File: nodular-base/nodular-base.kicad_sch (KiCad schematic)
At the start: 30 parts, among them J11 Conn_01x08_Pin, SW1 SW_Push, SW2 SW_Push, SW3 SW_Push, U1 ESP32-S3-PICO-1-N8R2

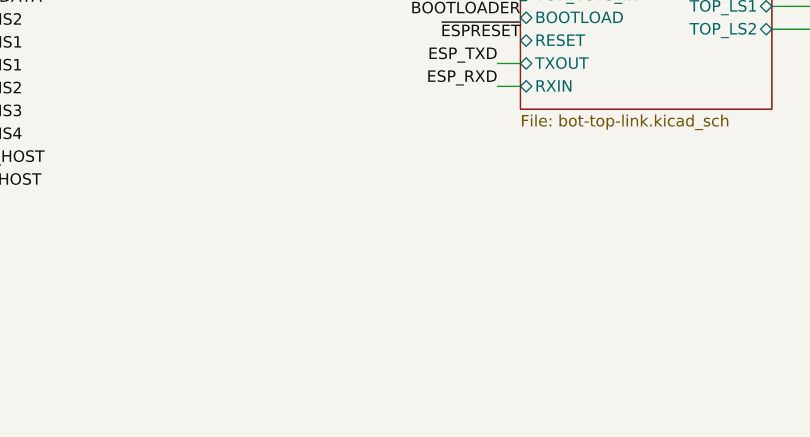
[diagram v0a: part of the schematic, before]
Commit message: Add baseline art (bart), add stencil alignment holes, complete BOM, prepare for proto order
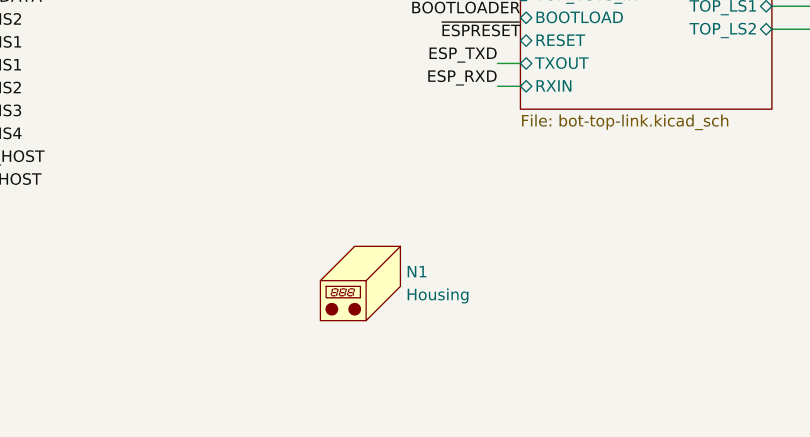
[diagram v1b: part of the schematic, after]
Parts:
- added N1: Housing, nodular:bartholomew, symbol Mechanical:Housing
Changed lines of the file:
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@@
+    )
+  )
+  (symbol (lib_id "Mechanical:Housing") (at 139.7 182.88 0) (unit 1)
+    (in_bom yes) (on_board yes) (dnp no) (fields_autoplaced)
+    (property "Reference" "N1" (at 143.51 181.9275 0)
+      (effects (font (size 1.27 1.27)) (justify left))
+    )
+    (property "Value" "Housing" (at 143.51 184.4675 0)
+      (effects (font (size 1.27 1.27)) (justify left))
+    )
+    (property "Footprint" "nodular:bartholomew" (at 140.97 181.61 0)
+      (effects (font (size 1.27 1.27)) hide)
+    )
+    (property "Datasheet" "~" (at 140.97 181.61 0)
+      (effects (font (size 1.27 1.27)) hide)
+    )
+    (instances
+      (project "nodular-base"
+        (path "/6dcb0502-87e2-4c28-9ce8-81aab8925f06"
+          (reference "N1") (unit 1)
+        )
+      )
     )
   )

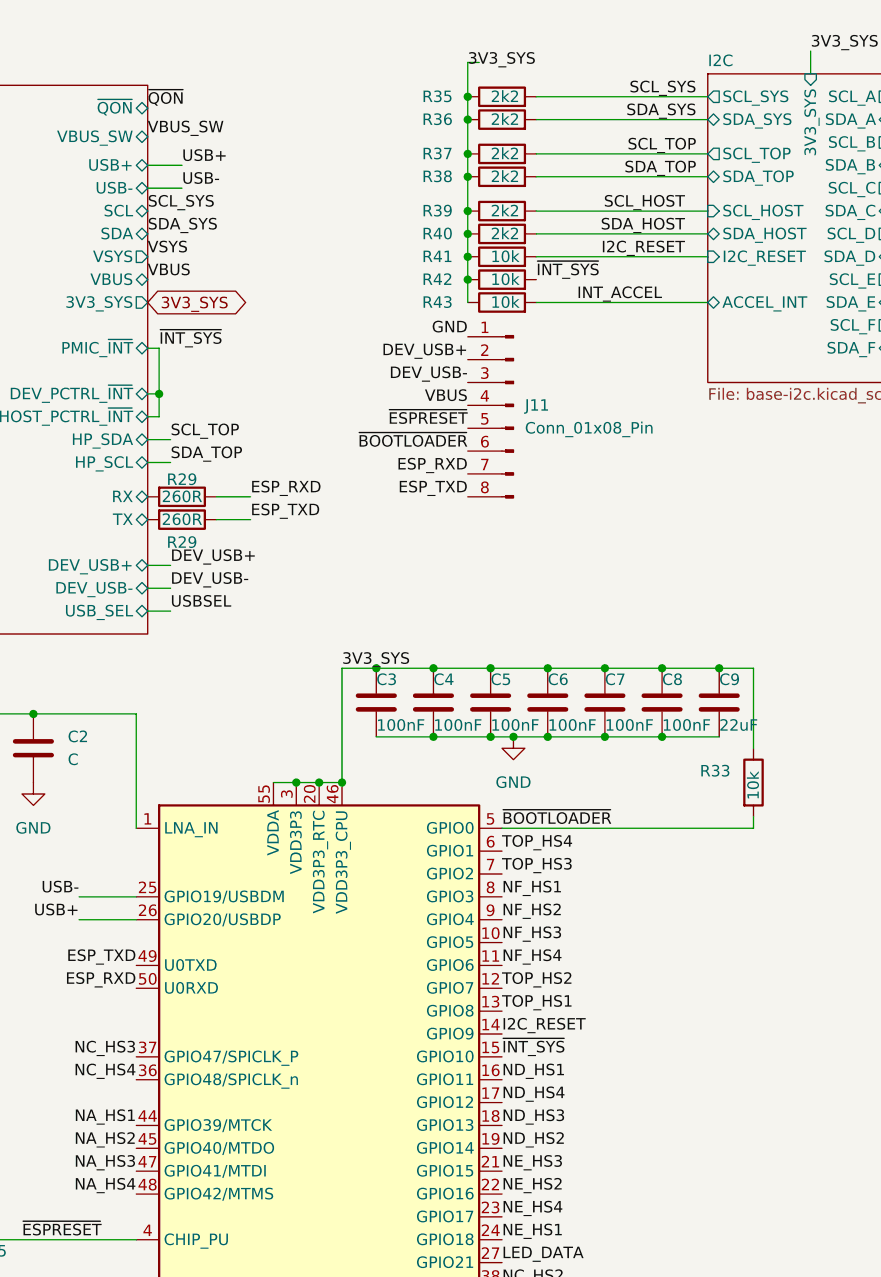
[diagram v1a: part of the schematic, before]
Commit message: Modify base board: - Fix ESP32 strapping pins state - Remove 3/6 M3 standoffs - Change to LGA-style pads on ESP32 - Modify SFP mechanical pads to not be plated - Add larger mechanical pads with more solder paste surface to USB-C connectors
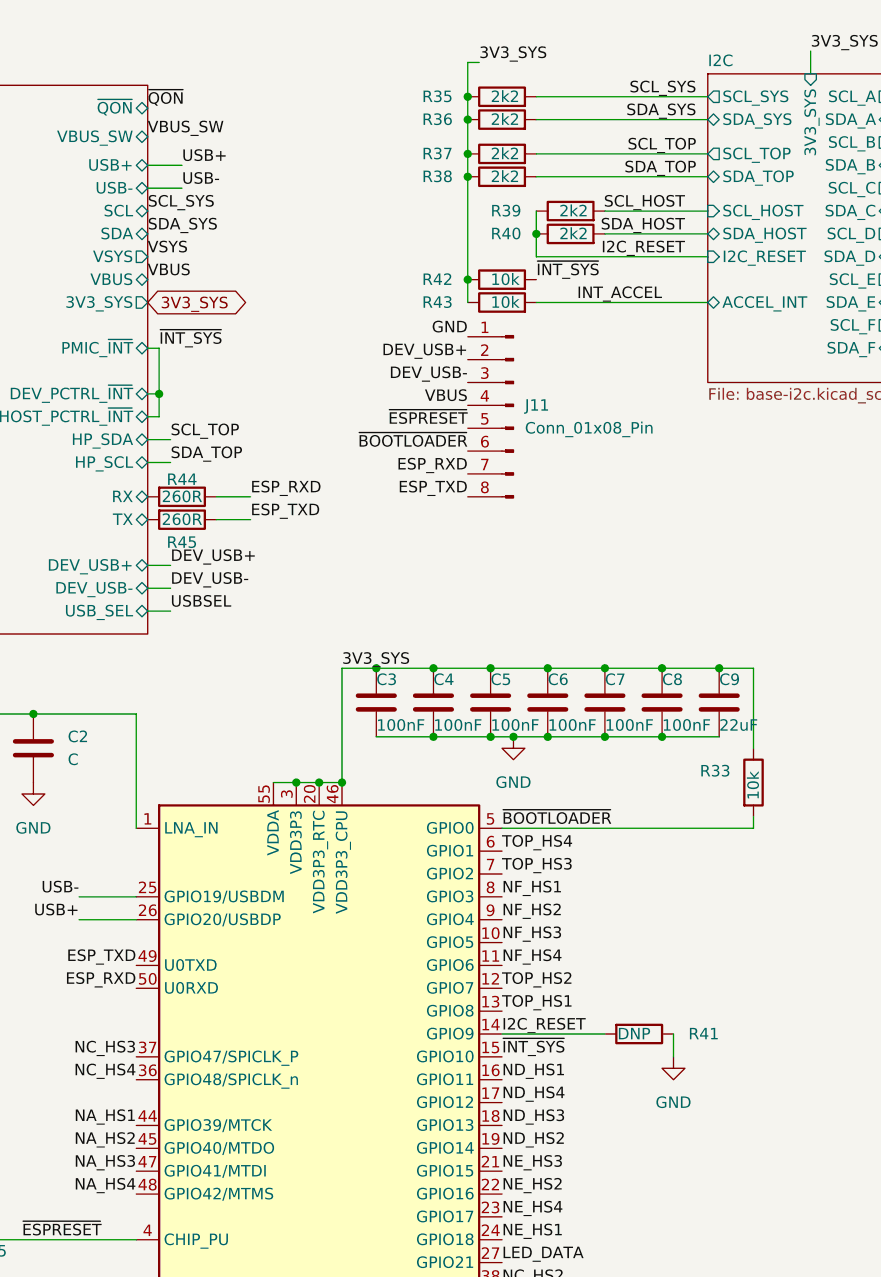
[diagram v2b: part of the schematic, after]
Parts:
- R41: value 10k -> DNP
- U1: footprint Package_DFN_QFN:QFN-56-1EP_7x7mm_P0.4mm_EP4x4mm -> nodular:LGA56-1EP_7x7mm_P0.4mm_EP4x4mm
- renumbered R29 to R44, R29 to R45
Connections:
- net 3V3_SYS: no longer R39.1, R40.1, R41.1
- net GND: now also R41.1
- net I2C_RESET: now also R39.1, R40.1
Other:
- moved on the sheet: R39, R40, R41
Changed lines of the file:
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@@
   (junction (at 76.2 99.06) (diameter 0) (color 0 0 0 0)
   )
-  (junction (at 90.17 38.1) (diameter 0) (color 0 0 0 0)
-  )
   (junction (at 105.41 93.98) (diameter 0) (color 0 0 0 0)
   )
@@
   (junction (at 90.17 22.86) (diameter 0) (color 0 0 0 0)
   )
-  (junction (at 90.17 35.56) (diameter 0) (color 0 0 0 0)
-  )
   (junction (at 111.76 93.98) (diameter 0) (color 0 0 0 0)
   )
   (junction (at 73.66 99.06) (diameter 0) (color 0 0 0 0)
   )
-  (junction (at 90.17 40.64) (diameter 0) (color 0 0 0 0)
-  )
   (junction (at 99.06 93.98) (diameter 0) (color 0 0 0 0)
   )
@@
   )
   (junction (at 86.36 86.36) (diameter 0) (color 0 0 0 0)
+  )
+  (junction (at 97.79 38.1) (diameter 0) (color 0 0 0 0)
   )
   (junction (at 118.11 86.36) (diameter 0) (color 0 0 0 0)
@@
     (stroke (width 0) (type default))
   )
+  (wire (pts (xy 97.79 38.1) (xy 97.79 40.64))
+    (stroke (width 0) (type default))
+  )
   (wire (pts (xy 92.71 93.98) (xy 95.25 93.98))
     (stroke (width 0) (type default))
@@
     (stroke (width 0) (type default))
   )
+  (wire (pts (xy 97.79 35.56) (xy 97.79 38.1))
+    (stroke (width 0) (type default))
+  )
   (wire (pts (xy 153.67 158.75) (xy 156.21 158.75))
     (stroke (width 0) (type default))
@@
     (stroke (width 0) (type default))
   )
-  (wire (pts (xy 97.79 35.56) (xy 116.84 35.56))
+  (wire (pts (xy 105.41 35.56) (xy 116.84 35.56))
     (stroke (width 0) (type default))
   )
@@
     (stroke (width 0) (type default))
   )
-  (wire (pts (xy 90.17 31.75) (xy 90.17 35.56))
-    (stroke (width 0) (type default))
-  )
   (wire (pts (xy 185.42 92.71) (xy 205.74 92.71))
     (stroke (width 0) (type default))
@@
     (stroke (width 0) (type default))
   )
+  (wire (pts (xy 113.03 127) (xy 113.03 129.54))
+    (stroke (width 0) (type default))
+  )
   (wire (pts (xy 184.15 149.86) (xy 205.74 149.86))
     (stroke (width 0) (type default))
@@
     (stroke (width 0) (type default))
   )
-  (wire (pts (xy 90.17 40.64) (xy 90.17 43.18))
+  (wire (pts (xy 90.17 31.75) (xy 90.17 43.18))
     (stroke (width 0) (type default))
   )
@@
     (stroke (width 0) (type default))
   )
-  (wire (pts (xy 97.79 38.1) (xy 116.84 38.1))
+  (wire (pts (xy 105.41 38.1) (xy 116.84 38.1))
     (stroke (width 0) (type default))
   )
@@
     (stroke (width 0) (type default))
   )
-  (wire (pts (xy 90.17 35.56) (xy 90.17 38.1))
-    (stroke (width 0) (type default))
-  )
   (wire (pts (xy 185.42 26.67) (xy 205.74 26.67))
     (stroke (width 0) (type default))
@@
     (stroke (width 0) (type default))
   )
-  (wire (pts (xy 90.17 38.1) (xy 90.17 40.64))
-    (stroke (width 0) (type default))
-  )
   (wire (pts (xy 137.16 50.8) (xy 157.48 50.8))
     (stroke (width 0) (type default))
@@
     (stroke (width 0) (type default))
   )
+  (wire (pts (xy 93.98 127) (xy 105.41 127))
+    (stroke (width 0) (type default))
+  )
   (wire (pts (xy 185.42 39.37) (xy 205.74 39.37))
     (stroke (width 0) (type default))
@@
     (effects (font (size 1.27 1.27)) (justify right bottom))
   )
-  (label "3V3_SYS" (at 90.17 19.685 0) (fields_autoplaced)
+  (label "3V3_SYS" (at 91.44 19.05 0) (fields_autoplaced)
     (effects (font (size 1.27 1.27)) (justify left bottom))
   )
@@
     )
   )
-  (symbol (lib_id "Device:R") (at 93.98 40.64 90) (unit 1)
-    (in_bom yes) (on_board yes) (dnp no)
-    (property "Reference" "R41" (at 85.09 40.64 90)
-      (effects (font (size 1.27 1.27)) (justify right))
-    )
-    (property "Value" "10k" (at 92.71 40.64 90)
-      (effects (font (size 1.27 1.27)) (justify right))
-    )
-    (property "Footprint" "Resistor_SMD:R_0402_1005Metric" (at 93.98 42.418 90)
-      (effects (font (size 1.27 1.27)) hide)
-    )
-    (property "Datasheet" "~" (at 93.98 40.64 0)
+  (symbol (lib_id "Device:R") (at 109.22 127 270) (unit 1)
+    (in_bom yes) (on_board yes) (dnp no)
+    (property "Reference" "R41" (at 118.11 127 90)
+      (effects (font (size 1.27 1.27)) (justify right))
+    )
+    (property "Value" "DNP" (at 110.49 127 90)
+      (effects (font (size 1.27 1.27)) (justify right))
+    )
+    (property "Footprint" "Resistor_SMD:R_0402_1005Metric" (at 109.22 125.222 90)
+      (effects (font (size 1.27 1.27)) hide)
+    )
+    (property "Datasheet" "~" (at 109.22 127 0)
       (effects (font (size 1.27 1.27)) hide)
     )
@@
   (symbol (lib_id "Device:R") (at 58.42 67.31 270) (unit 1)
     (in_bom yes) (on_board yes) (dnp no)
-    (property "Reference" "R29" (at 58.42 65.405 90)
+    (property "Reference" "R44" (at 58.42 65.405 90)
       (effects (font (size 1.27 1.27)))
     )
@@
     (instances
       (project "nodular-base"
-        (path "/6dcb0502-87e2-4c28-9ce8-81aab8925f06/febeaf27-8aaa-445d-863a-3f8ee5c51d55"
-          (reference "R29") (unit 1)
-        )
         (path "/6dcb0502-87e2-4c28-9ce8-81aab8925f06"
           (reference "R44") (unit 1)
@@
     )
   )
+  (symbol (lib_id "power:GND") (at 113.03 129.54 0) (unit 1)
+    (in_bom yes) (on_board yes) (dnp no) (fields_autoplaced)
+    (property "Reference" "#PWR072" (at 113.03 135.89 0)
+      (effects (font (size 1.27 1.27)) hide)
+    )
+    (property "Value" "GND" (at 113.03 134.62 0)
+      (effects (font (size 1.27 1.27)))
+    )
+    (property "Footprint" "" (at 113.03 129.54 0)
+      (effects (font (size 1.27 1.27)) hide)
+    )
+    (property "Datasheet" "" (at 113.03 129.54 0)
+      (effects (font (size 1.27 1.27)) hide)
+    )
+    (pin "1")
+    (instances
+      (project "nodular-base"
+        (path "/6dcb0502-87e2-4c28-9ce8-81aab8925f06"
+          (reference "#PWR072") (unit 1)
+        )
+      )
+    )
+  )
   (symbol (lib_id "Device:R") (at 93.98 43.18 90) (unit 1)
     (in_bom yes) (on_board yes) (dnp no)
@@
     )
   )
-  (symbol (lib_id "Device:R") (at 93.98 38.1 90) (unit 1)
-    (in_bom yes) (on_board yes) (dnp no)
-    (property "Reference" "R40" (at 85.09 38.1 90)
-      (effects (font (size 1.27 1.27)) (justify right))
-    )
-    (property "Value" "2k2" (at 92.71 38.1 90)
-      (effects (font (size 1.27 1.27)) (justify right))
-    )
-    (property "Footprint" "Resistor_SMD:R_0402_1005Metric" (at 93.98 39.878 90)
-      (effects (font (size 1.27 1.27)) hide)
-    )
-    (property "Datasheet" "~" (at 93.98 38.1 0)
+  (symbol (lib_id "Device:R") (at 101.6 38.1 90) (unit 1)
+    (in_bom yes) (on_board yes) (dnp no)
+    (property "Reference" "R40" (at 92.71 38.1 90)
+      (effects (font (size 1.27 1.27)) (justify right))
+    )
+    (property "Value" "2k2" (at 100.33 38.1 90)
+      (effects (font (size 1.27 1.27)) (justify right))
+    )
+    (property "Footprint" "Resistor_SMD:R_0402_1005Metric" (at 101.6 39.878 90)
+      (effects (font (size 1.27 1.27)) hide)
+    )
+    (property "Datasheet" "~" (at 101.6 38.1 0)
       (effects (font (size 1.27 1.27)) hide)
     )
@@
       (effects (font (size 1.27 1.27)) (justify left))
     )
-    (property "Footprint" "Package_DFN_QFN:QFN-56-1EP_7x7mm_P0.4mm_EP4x4mm" (at 73.66 182.88 0)
+    (property "Footprint" "nodular:LGA56-1EP_7x7mm_P0.4mm_EP4x4mm" (at 73.66 182.88 0)
       (effects (font (size 1.27 1.27)) hide)
     )
@@
     )
   )
-  (symbol (lib_id "Device:R") (at 93.98 35.56 90) (unit 1)
-    (in_bom yes) (on_board yes) (dnp no)
-    (property "Reference" "R39" (at 85.09 35.56 90)
-      (effects (font (size 1.27 1.27)) (justify right))
-    )
-    (property "Value" "2k2" (at 92.71 35.56 90)
-      (effects (font (size 1.27 1.27)) (justify right))
-    )
-    (property "Footprint" "Resistor_SMD:R_0402_1005Metric" (at 93.98 37.338 90)
-      (effects (font (size 1.27 1.27)) hide)
-    )
-    (property "Datasheet" "~" (at 93.98 35.56 0)
+  (symbol (lib_id "Device:R") (at 101.6 35.56 90) (unit 1)
+    (in_bom yes) (on_board yes) (dnp no)
+    (property "Reference" "R39" (at 92.71 35.56 90)
+      (effects (font (size 1.27 1.27)) (justify right))
+    )
+    (property "Value" "2k2" (at 100.33 35.56 90)
+      (effects (font (size 1.27 1.27)) (justify right))
+    )
+    (property "Footprint" "Resistor_SMD:R_0402_1005Metric" (at 101.6 37.338 90)
+      (effects (font (size 1.27 1.27)) hide)
+    )
+    (property "Datasheet" "~" (at 101.6 35.56 0)
       (effects (font (size 1.27 1.27)) hide)
     )
@@
   (symbol (lib_id "Device:R") (at 58.42 69.85 270) (unit 1)
     (in_bom yes) (on_board yes) (dnp no)
-    (property "Reference" "R29" (at 58.42 72.39 90)
+    (property "Reference" "R45" (at 58.42 72.39 90)
       (effects (font (size 1.27 1.27)))
     )
@@
     (instances
       (project "nodular-base"
-        (path "/6dcb0502-87e2-4c28-9ce8-81aab8925f06/febeaf27-8aaa-445d-863a-3f8ee5c51d55"
-          (reference "R29") (unit 1)
-        )
         (path "/6dcb0502-87e2-4c28-9ce8-81aab8925f06"
           (reference "R45") (unit 1)

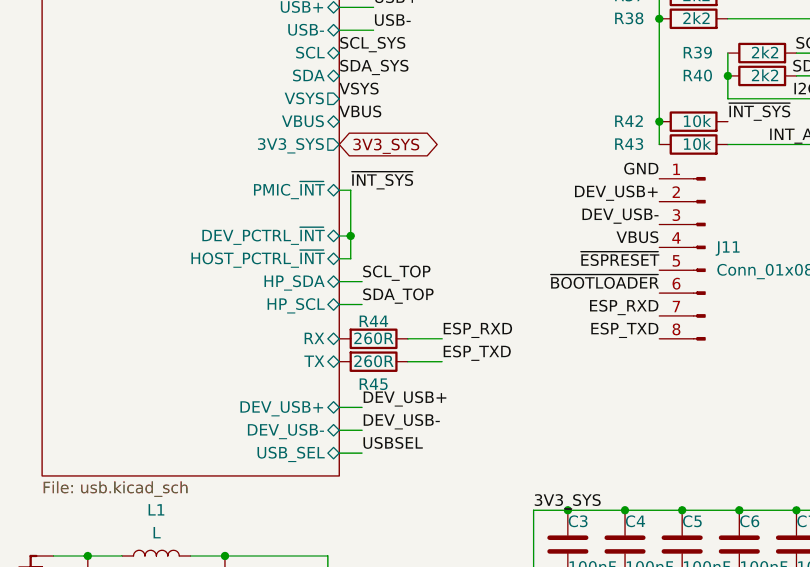
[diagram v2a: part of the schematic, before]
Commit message: Update top board layout, rename libraries
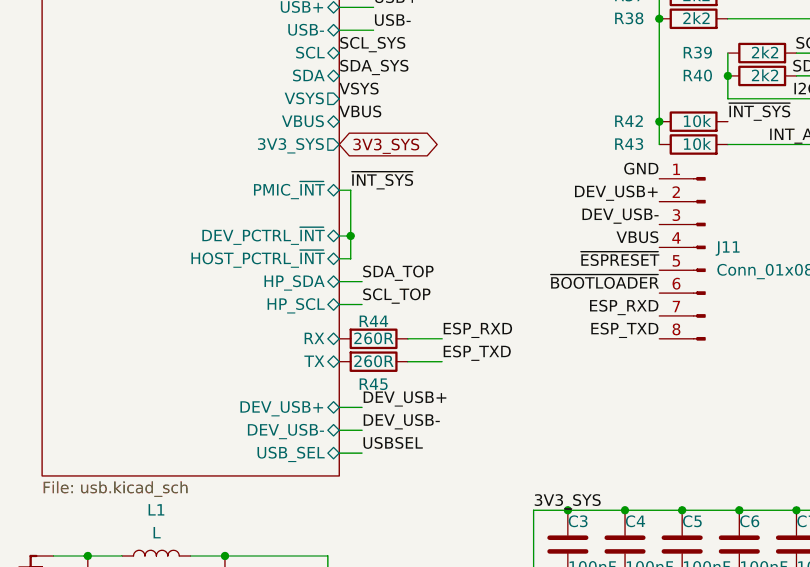
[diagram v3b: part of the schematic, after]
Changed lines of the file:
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@@
     (effects (font (size 1.27 1.27)) (justify right bottom))
   )
-  (label "SDA_TOP" (at 57.15 63.5 0) (fields_autoplaced)
+  (label "SDA_TOP" (at 57.15 60.96 0) (fields_autoplaced)
     (effects (font (size 1.27 1.27)) (justify left bottom))
   )
@@
     (effects (font (size 1.27 1.27)) (justify left bottom))
   )
-  (label "SCL_TOP" (at 57.15 60.96 0) (fields_autoplaced)
-    (effects (font (size 1.27 1.27)) (justify left bottom))
-  )
+  (label "SCL_TOP" (at 57.15 63.5 0) (fields_autoplaced)
+    (effects (font (size 1.27 1.27)) (justify left bottom))
+  )
